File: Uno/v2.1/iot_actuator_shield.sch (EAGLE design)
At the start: 6 parts, among them IC1 REG1117, U1 ARDUINOR3-DIMENSION

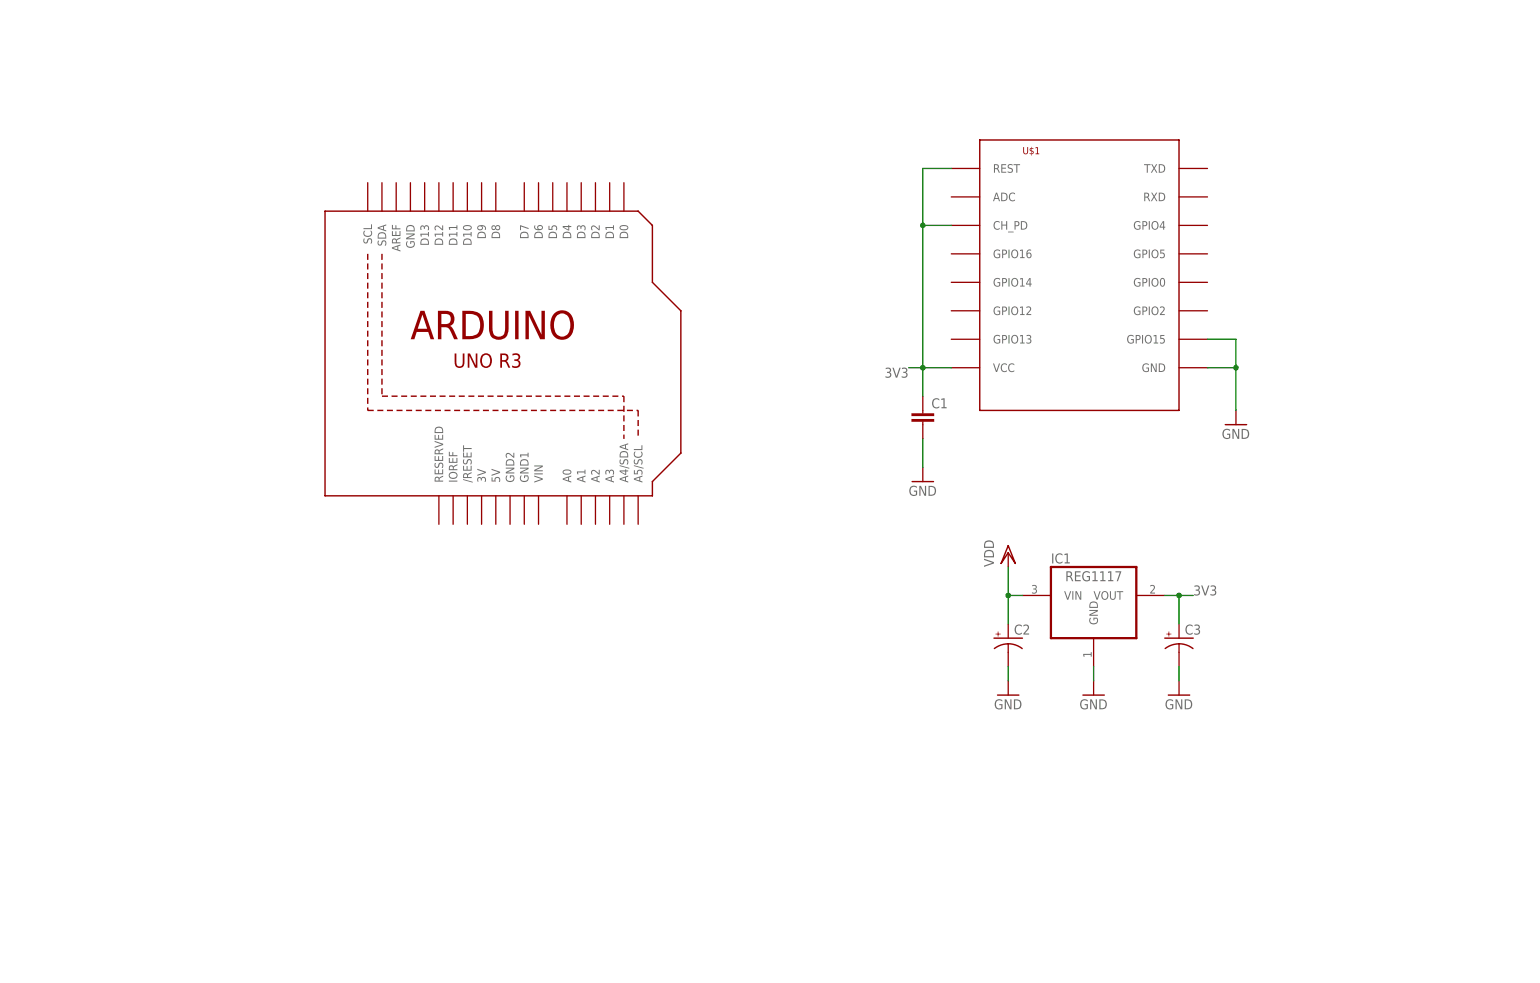
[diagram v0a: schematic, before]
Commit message: IO-Expander and Darlington array
the output circuitry is added to schematics (copied
from the ThermoShield project)
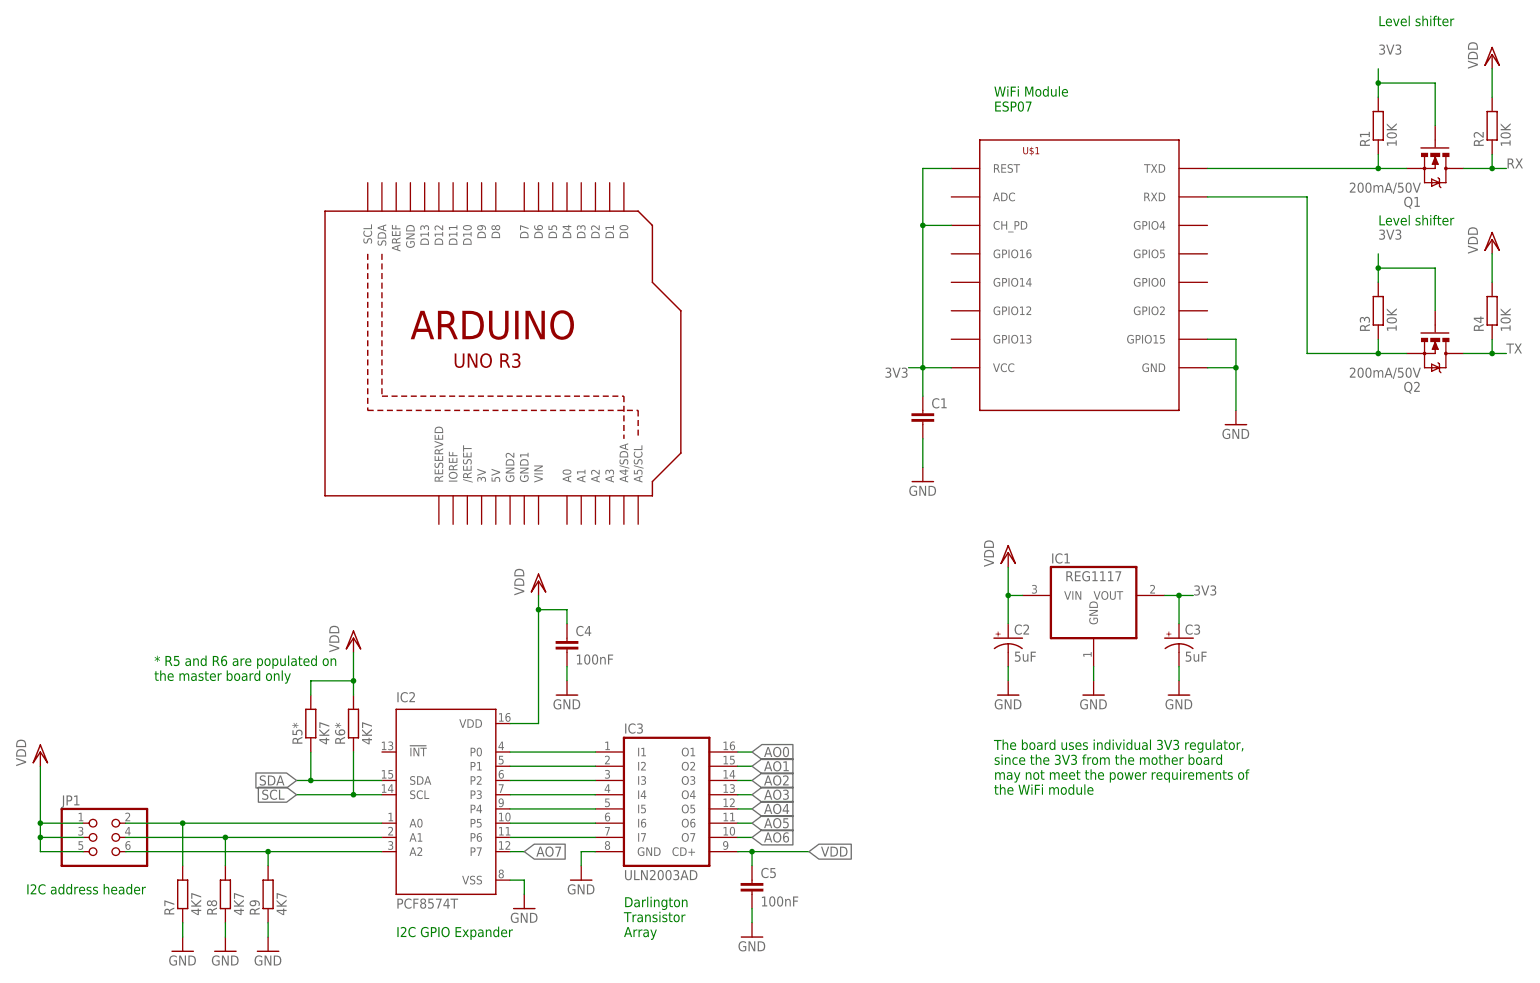
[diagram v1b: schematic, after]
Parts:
- added C4, C5: 100nF, rcl:C-EUC0805
- added IC2: PCF8574T, micro-philips:PCF8574T
- added IC3: ULN2003AD, uln-udn:ULN2003AD
- added JP1: (no value), pinhead:PINHD-2X3
- added Q1, Q2: 200mA/50V, SparkFun-DiscreteSemi:MOSFET-NCHANNELBSS138
- added R1, R2, R3, R4: 10K, resistor:R-EU_M0805
- added R5*, R6*, R7, R8, R9: 4K7, resistor:R-EU_M0805
- C2, C3: value (none) -> 5uF
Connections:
- new net AO0: IC3.O1
- new net AO1: IC3.O2
- new net AO2: IC3.O3
- new net AO3: IC3.O4
- new net AO4: IC3.O5
- new net AO5: IC3.O6
- new net AO6: IC3.O7
- new net AO7: IC2.P7
- new net N$1: Q2.S, R3.1, U$1.RXD
- new net N$10: IC2.A0, JP1.2, R7.2
- new net N$11: IC2.A1, JP1.4, R8.2
- new net N$12: IC2.A2, JP1.6, R9.2
- new net N$2: Q1.S, R1.1, U$1.TXD
- new net N$3: IC2.P0, IC3.I1
- new net N$4: IC2.P1, IC3.I2
- new net N$5: IC2.P2, IC3.I3
- new net N$6: IC2.P3, IC3.I4
- new net N$7: IC2.P4, IC3.I5
- new net N$8: IC2.P5, IC3.I6
- new net N$9: IC2.P6, IC3.I7
- new net RX: Q1.D, R2.1
- new net SCL: IC2.SCL, R6*.1
- new net SDA: IC2.SDA, R5*.1
- new net TX: Q2.D, R4.1
- net 3V3: now also Q1.G, Q2.G, R1.2, R3.2
- net GND: now also C4.2, C5.2, IC2.VSS, IC3.GND, R7.1, R8.1, R9.1
- net VDD: now also C4.1, C5.1, IC2.VDD, IC3.CD+, JP1.1, JP1.3, JP1.5, R2.2, R4.2, R5*.2, R6*.2
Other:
- note added: "* R5 and R6 are populated on the master board only"
- note added: "Darlington Transistor Array"
- note added: "I2C GPIO Expander"
- note added: "I2C address header"
- note added: "Level shifter"
- note added: "The board uses individual 3V3 regulator, since the 3V3 from the mother board may not meet the power requirements of the WiFi module"
- note added: "WiFi Module ESP07"

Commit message: shield added
most components added including the shield
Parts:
- removed C2, C3: 5uF, SparkFun-Capacitors:CAP_POL1206
- removed C4, C5: 100nF, rcl:C-EUC0805
- removed R1, R2, R3, R4: 10K, resistor:R-EU_M0805
- removed R5*, R6*: 4K7, resistor:R-EU_M0805
- removed U$1: ESP8266-07, lio:ESP8266-07
- added 1, 2, 3, 4, 5, 6, 7, 8: (no value), led:LEDCHIP-LED0805
- added ANALOG: (no value), pinhead:PINHD-1X6
- added C10, C13, C14, C9: 100nF, rcl:C-EUC0805
- added C11, C12, C8: 5uF, SparkFun-Capacitors:CAP_POL1206
- added FRAME1, FRAME2: FRAME-LETTER, SparkFun-Aesthetics:FRAME-LETTER
- added J1, J2: (no value), SmartPrj:PINHD-1X8TH
- added J3: (no value), SmartPrj:PINHD-1X10TH
- added JP5: (no value), pinhead:PINHD-2X3
- added LED9: Blue, led:LEDCHIP-LED0805
- added MISHA1: ESP8266-07, lio:ESP8266-07
- added R10, R11, R12, R14, R15, R16, R22: 3K3, rcl:R-EU_R0805
- added R13: 1K, rcl:R-EU_R1206
- added R23, R24, R25, R26: 10K, rcl:R-EU_R0805
- added R5, R6: 1K, rcl:R-EU_R0805
- added R8*, R9*: 4K7, rcl:R-EU_R0805
- added U2: AD5165BUJZ100-R2, AD5165_DigitalPot:AD5165BUJZ100-R2
- added X1: (no value), con-phoenix-500:MSTBV8
- added X10, X11, X2, X3, X4, X5, X6, X7, X8, X9: (no value), con-phoenix-500:MSTBV2
- C1: value (none) -> 100nF
- IC1: value REG1117 -> PCF8574T; device burr-brown:REG1117 -> micro-philips:PCF8574T
- IC2: value PCF8574T -> ULN2003AD; device micro-philips:PCF8574T -> uln-udn:ULN2003AD
- IC3: value ULN2003AD -> REG1117; device uln-udn:ULN2003AD -> burr-brown:REG1117
- JP1: device pinhead:PINHD-2X3 -> pinhead:PINHD-2X4
- R7: value 4K7 -> 1K; device resistor:R-EU_M0805 -> rcl:R-EU_R0805
- R8, R9: value 4K7 -> 3K3; device resistor:R-EU_M0805 -> rcl:R-EU_R0805
- U1: value ARDUINOR3-DIMENSION -> CD74HCT4051_D_16; device adafruit:ARDUINOR3-DIMENSION -> misha-74HCT4051:CD74HCT4051_D_16
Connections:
- removed net N$12: IC2.A2, JP1.6, R9.2
- new net A0: ANALOG.1, JP1.1
- new net A1: ANALOG.2, JP1.3
- new net A2: ANALOG.3, JP1.5
- new net A3: ANALOG.4, JP1.7
- new net AS0: U1.A0, X4-1.SK
- new net AS1: U1.A1, X5-1.SK
- new net AS2: U1.A2, X6-1.SK
- new net AS3: U1.A3, X7-1.SK
- new net AS4: U1.A4, X8-1.SK
- new net AS5: U1.A5, X9-1.SK
- new net AS6: U1.A6, X10-1.SK
- new net AS7: U1.A7, X11-1.SK
- new net D10: U1.S2
- new net D11: U2.CS
- new net D51(MOSI): U2.SDI
- new net D52(SCLK): U2.CLK
- new net D8: U1.S0
- new net D9: U1.S1
- new net N$126: LED9.A, R22.1
- new net N$23: 2.A, R9.1
- new net N$24: IC1.A1, JP5.4, R6.1
- new net N$25: IC1.A2, JP5.6, R7.1
- new net N$32: 3.A, R10.1
- new net N$36: C8.+, R13.1
- new net N$40: MISHA1.TXD, Q1.S, R23.1
- new net N$41: MISHA1.RXD, Q2.S, R24.1
- new net N$46: 4.A, R11.1
- new net N$47: 5.A, R12.1
- new net N$48: 6.A, R14.1
- new net N$49: 7.A, R15.1
- new net N$50: 8.A, R16.1
- net 3V3: now also C12.+, C13.1, IC3.VOUT, MISHA1.CH_PD, MISHA1.REST, MISHA1.VCC, R23.2, R24.2; no longer C1.1, C3.+, IC1.VOUT, R1.2, R3.2, U$1.CH_PD, U$1.REST, U$1.VCC
- net AO0: now also 1.C, IC2.O1, X1-8.SK; no longer IC3.O1
- net AO1: now also 2.C, IC2.O2, X1-7.SK; no longer IC3.O2
- net AO2: now also 3.C, IC2.O3, X1-6.SK; no longer IC3.O3
- net AO3: now also 4.C, IC2.O4, X1-5.SK; no longer IC3.O4
- net AO4: now also 5.C, IC2.O5, X1-4.SK; no longer IC3.O5
- net AO5: now also 6.C, IC2.O6, X1-3.SK; no longer IC3.O6
- net AO6: now also 7.C, IC2.O7, X1-2.SK; no longer IC3.O7
- net AO7: now also 8.C, IC1.P7, X1-1.SK; no longer IC2.P7
- net GND: now also C10.2, C11.-, C12.-, C13.2, C14.2, C8.-, C9.2, IC1.VSS, IC2.GND, JP5.1, JP5.3, JP5.5, LED9.C, MISHA1.GND, MISHA1.GPIO15, U1.*E, U1.GND, U1.VEE, U2.GND, X10-2.SK, X11-2.SK, X3-1.SK, X3-2.SK, X4-2.SK, X5-2.SK, X6-2.SK, X7-2.SK, X8-2.SK, X9-2.SK; no longer C2.-, C3.-, C4.2, C5.2, IC1.GND, IC2.VSS, R7.1, R8.1, R9.1, U$1.GND, U$1.GPIO15
- net N$1: now also JP1.2, JP1.4, JP1.6, JP1.8; no longer Q2.S, R3.1, U$1.RXD
- net N$10: now also IC1.A0, JP5.2, R5.1; no longer IC2.A0, JP1.2, R7.2
- net N$11: now also 1.A, R8.1; no longer IC2.A1, JP1.4, R8.2
- net N$2: now also R13.2, U1.A, U2.W; no longer Q1.S, R1.1, U$1.TXD
- net N$3: now also IC1.P0, IC2.I1; no longer IC2.P0, IC3.I1
- net N$4: now also IC1.P1, IC2.I2; no longer IC2.P1, IC3.I2
- net N$5: now also IC1.P2, IC2.I3; no longer IC2.P2, IC3.I3
- net N$6: now also IC1.P3, IC2.I4; no longer IC2.P3, IC3.I4
- net N$7: now also IC1.P4, IC2.I5; no longer IC2.P4, IC3.I5
- net N$8: now also IC1.P5, IC2.I6; no longer IC2.P5, IC3.I6
- net N$9: now also IC1.P6, IC2.I7; no longer IC2.P6, IC3.I7
- net RX: now also J1.1, R25.1; no longer R2.1
- net SCL: now also ANALOG.6, IC1.SCL, R9*.1; no longer IC2.SCL, R6*.1
- net SDA: now also ANALOG.5, IC1.SDA, R8*.1; no longer IC2.SDA, R5*.1
- net TX: now also J1.2, R26.1; no longer R4.1
- net VDD: now also C1.1, C10.1, C11.+, C14.1, C9.1, IC1.VDD, IC2.CD+, IC3.VIN, R10.2, R11.2, R12.2, R14.2, R15.2, R16.2, R22.2, R25.2, R26.2, R5.2, R6.2, R7.2, R8*.2, R8.2, R9*.2, R9.2, U1.VCC, U2.A, U2.VDD, X2-1.SK, X2-2.SK; no longer C2.+, C4.1, C5.1, IC1.VIN, IC2.VDD, IC3.CD+, JP1.1, JP1.3, JP1.5, R2.2, R4.2, R5*.2, R6*.2
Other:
- note added: "* R8 and R9 are populated on the master board only"
- note added: "256-step Digital pot Voltage Divider"
- note added: "8ch Multiplexer"
- note added: "Analog Input Selector (use one strap only)"
- note added: "Components on this sheet are populated on the master board only"
- note added: "Low-Pass Filter"
- note added: "Output signal LEDs. The LEDs and the current limitting resistors are only mounted if the standard blue terminals are used. For the 90 degree terminals, leave unpopulated"
- note added: "Power LED"
- note added: "Two extra contacts for VDD and GND primarily to connect the relay board"
- note added: "switch control"
- note removed: "* R5 and R6 are populated on the master board only"
- moved on the sheet: C1, Q1, Q2, R7, R8, R9
